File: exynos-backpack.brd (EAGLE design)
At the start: 29 x 52 mm, 17 parts, among them IC1 MIC5335-SPYMT, IC2 TXB0108RGY

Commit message: Route serial section
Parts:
- moved C13 9.41 mm to (18.7, 38.9), turned to 0 degrees
- moved C14 9.03 mm to (21.2, 38.9), turned to 0 degrees
- moved IC1 5.97 mm to (20.0, 36.4), turned to 0 degrees
- moved C12 3.95 mm to (20.0, 34.0), turned to 180 degrees
- moved JP4 3.05 mm to (3.81, 29.0)
- moved JP5 2.13 mm to (25.5, 32.9)
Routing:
- net 1.8V: track 0.00 -> 33.6 mm, vias 0 -> 2
- net ODROID_TXD: track 0.00 -> 26.1 mm
- net ODROID_RXD: track 0.00 -> 20.7 mm
- net V_BATT: track 0.00 -> 6.16 mm
- net 3.3V: track 0.00 -> 5.82 mm
- net IMAGEPROC_RXD: track 0.00 -> 4.09 mm
- net IMAGEPROC_TXD: track 0.00 -> 4.05 mm
- net 3.0V: track 0.00 -> 2.10 mm

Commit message: Delete inner layers
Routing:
- removed copper zone on layer 2, net GND
- removed copper zone on layer 3, net V_BATT

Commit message: Routing complete
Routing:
- net V_BATT: track 6.16 -> 25.2 mm
- added copper zone on layer 1, net 5V
- added copper zone on layer 16, net 5V
- added copper zone on layer 1, net V_BATT
- added copper zone on layer 16, net V_BATT
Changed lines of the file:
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@@
 <setting verticaltext="up"/>
 </settings>
-<grid distance="3" unitdist="mil" unit="mil" style="lines" multiple="1" display="yes" altdistance="1" altunitdist="mil" altunit="mil"/>
+<grid distance="6" unitdist="mil" unit="mil" style="lines" multiple="1" display="yes" altdistance="1" altunitdist="mil" altunit="mil"/>
 <layers>
 <layer number="1" name="Top" color="4" fill="1" visible="yes" active="yes"/>
@@
 <layer number="49" name="Reference" color="7" fill="1" visible="no" active="yes"/>
 <layer number="50" name="dxf" color="7" fill="1" visible="no" active="yes"/>
-<layer number="51" name="tDocu" color="6" fill="1" visible="yes" active="yes"/>
-<layer number="52" name="bDocu" color="7" fill="1" visible="yes" active="yes"/>
+<layer number="51" name="tDocu" color="6" fill="1" visible="no" active="yes"/>
+<layer number="52" name="bDocu" color="7" fill="1" visible="no" active="yes"/>
 <layer number="53" name="tGND_GNDA" color="7" fill="9" visible="no" active="no"/>
 <layer number="54" name="bGND_GNDA" color="1" fill="9" visible="no" active="no"/>
@@
 <contactref element="C15" pad="2"/>
 <contactref element="C16" pad="2"/>
-<polygon width="0.1524" layer="1">
+<polygon width="0.1524" layer="1" rank="6">
 <vertex x="0" y="52"/>
 <vertex x="30.524" y="52"/>
@@
 <vertex x="0" y="9"/>
 </polygon>
-<polygon width="0.1524" layer="16">
+<polygon width="0.1524" layer="16" rank="6">
 <vertex x="0" y="52"/>
-<vertex x="35.096" y="52"/>
-<vertex x="35.096" y="22"/>
+<vertex x="32.048" y="52"/>
+<vertex x="32.048" y="22"/>
 <vertex x="25" y="22"/>
 <vertex x="25" y="0"/>
@@
 <contactref element="JP5" pad="4"/>
 <via x="7.4676" y="49.2252" extent="1-16" drill="0.6" shape="square"/>
+<polygon width="0.1524" layer="1" thermals="no" rank="2">
+<vertex x="0" y="31.5468"/>
+<vertex x="24.9936" y="31.5468"/>
+<vertex x="24.9936" y="5.4864"/>
+<vertex x="15.0876" y="5.4864"/>
+<vertex x="15.0876" y="8.9916"/>
+<vertex x="0" y="8.9916"/>
+</polygon>
+<polygon width="0.1524" layer="16" thermals="no" rank="2">
+<vertex x="0" y="31.5468"/>
+<vertex x="24.9936" y="31.5468"/>
+<vertex x="24.9936" y="5.4864"/>
+<vertex x="15.0876" y="5.4864"/>
+<vertex x="15.0876" y="8.9916"/>
+<vertex x="0" y="8.9916"/>
+</polygon>
 </signal>
 <signal name="1.8V">
@@
 <wire x1="20.4644" y1="34.8662" x2="20.3454" y2="34.7472" width="0.254" layer="1"/>
 <wire x1="20.3454" y1="34.7472" x2="19.4644" y2="34.7472" width="0.254" layer="1"/>
-<wire x1="22.0218" y1="17.2847" x2="19.4818" y2="33.9852" width="0" layer="19" extent="1-1"/>
-<wire x1="22.174" y1="14.1732" x2="22.0218" y2="17.2847" width="0" layer="19" extent="16-16"/>
+<wire x1="19.4818" y1="33.9852" x2="19.4818" y2="29.3878" width="0.508" layer="1"/>
+<wire x1="19.4818" y1="29.3878" x2="17.9832" y2="27.8892" width="0.508" layer="1"/>
+<wire x1="17.9832" y1="27.8892" x2="17.9832" y2="21.3233" width="0.508" layer="1"/>
+<wire x1="17.9832" y1="21.3233" x2="22.0218" y2="17.2847" width="0.508" layer="1"/>
+<polygon width="0.1524" layer="16" thermals="no">
+<vertex x="20.1168" y="6.858"/>
+<vertex x="20.7264" y="6.2484"/>
+<vertex x="24.9936" y="6.2484"/>
+<vertex x="24.9936" y="18.5928"/>
+<vertex x="21.336" y="18.5928"/>
+<vertex x="20.7264" y="17.9832"/>
+<vertex x="20.7264" y="12.3444"/>
+<vertex x="23.4696" y="12.3444"/>
+<vertex x="23.4696" y="9.4488"/>
+<vertex x="21.0312" y="9.4488"/>
+<vertex x="20.1168" y="8.5344"/>
+</polygon>
+<polygon width="0.1524" layer="1" thermals="no">
+<vertex x="20.1168" y="6.858"/>
+<vertex x="20.7264" y="6.2484"/>
+<vertex x="24.9936" y="6.2484"/>
+<vertex x="24.9936" y="18.5928"/>
+<vertex x="21.336" y="18.5928"/>
+<vertex x="20.7264" y="17.9832"/>
+<vertex x="20.7264" y="12.3444"/>
+<vertex x="23.4696" y="12.3444"/>
+<vertex x="23.4696" y="9.4488"/>
+<vertex x="21.0312" y="9.4488"/>
+<vertex x="20.1168" y="8.5344"/>
+</polygon>
 </signal>
 <signal name="3.3V">
@@
 <contactref element="PS1" pad="4"/>
 <contactref element="JP4" pad="2"/>
-<wire x1="5.5628" y1="11.1252" x2="6.96" y2="30.206" width="0" layer="19" extent="16-16"/>
-<wire x1="2.9718" y1="10.9347" x2="5.5628" y2="11.1252" width="0" layer="19" extent="16-16"/>
+<polygon width="0.1524" layer="1" thermals="no">
+<vertex x="7.7724" y="28.956"/>
+<vertex x="5.7912" y="28.956"/>
+<vertex x="4.4196" y="27.5844"/>
+<vertex x="4.4196" y="8.9916"/>
+<vertex x="0" y="8.9916"/>
+<vertex x="0" y="31.5468"/>
+<vertex x="7.7724" y="31.5468"/>
+<vertex x="8.382" y="30.9372"/>
+<vertex x="8.382" y="29.5656"/>
+</polygon>
+<polygon width="0.1524" layer="16" thermals="no">
+<vertex x="6.858" y="12.192"/>
+<vertex x="6.2484" y="12.8016"/>
+<vertex x="1.8288" y="12.8016"/>
+<vertex x="1.2192" y="12.192"/>
+<vertex x="1.2192" y="8.9916"/>
+<vertex x="6.858" y="8.9916"/>
+</polygon>
+<polygon width="0.1524" layer="16" thermals="no">
+<vertex x="7.7724" y="28.956"/>
+<vertex x="5.7912" y="28.956"/>
+<vertex x="4.4196" y="27.5844"/>
+<vertex x="4.4196" y="8.9916"/>
+<vertex x="0" y="8.9916"/>
+<vertex x="0" y="31.5468"/>
+<vertex x="7.7724" y="31.5468"/>
+<vertex x="8.382" y="30.9372"/>
+<vertex x="8.382" y="29.5656"/>
+</polygon>
 </signal>
 <signal name="ODROID_TXD">

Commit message: Arrange silkscreen
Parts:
- removed C14: 1uF, biomimetic:0402-CAP
- JP1: value ODROID -> ODROID UART; device biomimetic:1X04_MOLEX_5267 -> biomimetic:1X04_MOLEX_5267_NOSILK
- JP3: value JST-RCY-MALE-NOSILK -> BATTERY
- JP4: value JST-RCY-FEMALE-NOSILK -> ODROID 5V
- JP5: value ODROID CONSOLE -> CONSOLE
- moved U$12 66.9 mm to (7.47, 45.9)
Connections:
- removed net 3.0V: C14.1, IC1.5
- net GND: now also IC1.3; no longer C14.2
- net V_BATT: no longer IC1.3
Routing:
- net 3.0V: track 2.10 -> 0.00 mm
- net V_BATT: track 25.2 -> 24.5 mm
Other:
- board text added: "Biomimetic Millisystems Laboratory"
- board text added: "Design by: Ryan Julian"
- board text added: "Exynos Backpack v1.0 Rev. A 2013.02.27"
- board text removed: "2013.02.16"
- board text removed: "Biomimetic"
- board text removed: "Exynos Backpack 1.0 Rev. A"
- board text removed: "Laboratory"
- board text removed: "Millisystems"
- board text removed: "Ryan Julian"

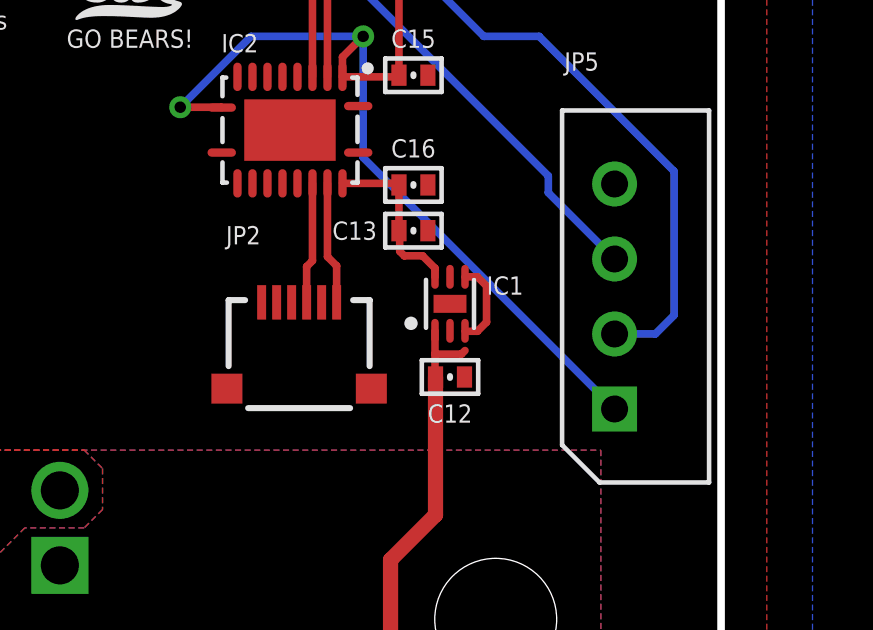
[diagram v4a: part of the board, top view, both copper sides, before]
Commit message: Disable 3.0v supply
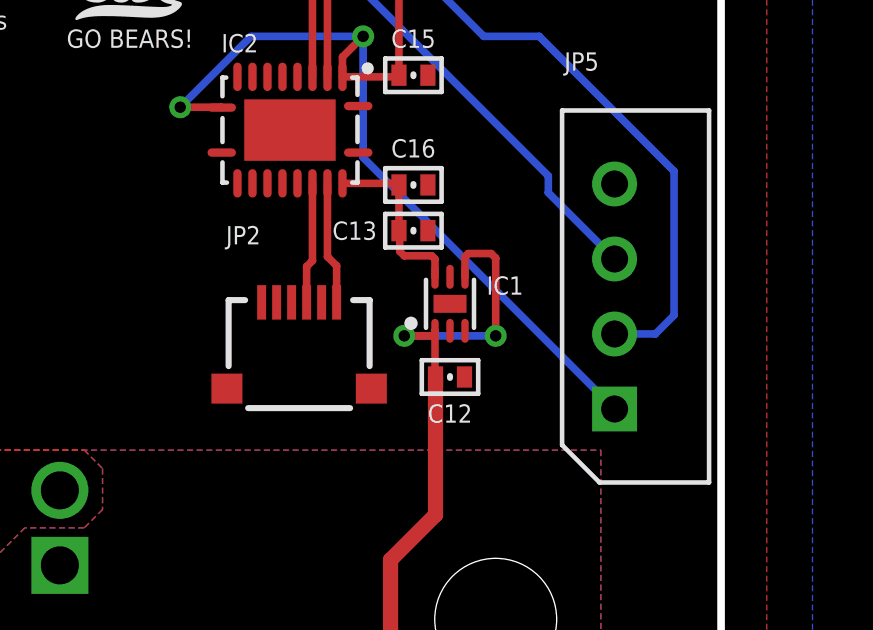
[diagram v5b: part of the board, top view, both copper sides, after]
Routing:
- net V_BATT: track 24.5 -> 29.2 mm, vias 0 -> 2
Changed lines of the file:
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@@
 <grid distance="6" unitdist="mil" unit="mil" style="lines" multiple="1" display="yes" altdistance="1" altunitdist="mil" altunit="mil"/>
 <layers>
-<layer number="1" name="Top" color="4" fill="1" visible="no" active="yes"/>
+<layer number="1" name="Top" color="4" fill="1" visible="yes" active="yes"/>
 <layer number="2" name="Route2" color="1" fill="3" visible="no" active="yes"/>
 <layer number="3" name="Route3" color="4" fill="3" visible="no" active="yes"/>
@@
 <layer number="14" name="Route14" color="1" fill="6" visible="no" active="no"/>
 <layer number="15" name="Route15" color="4" fill="6" visible="no" active="no"/>
-<layer number="16" name="Bottom" color="1" fill="1" visible="no" active="yes"/>
+<layer number="16" name="Bottom" color="1" fill="1" visible="yes" active="yes"/>
 <layer number="17" name="Pads" color="2" fill="1" visible="no" active="yes"/>
-<layer number="18" name="Vias" color="2" fill="1" visible="no" active="yes"/>
-<layer number="19" name="Unrouted" color="6" fill="1" visible="no" active="yes"/>
+<layer number="18" name="Vias" color="2" fill="1" visible="yes" active="yes"/>
+<layer number="19" name="Unrouted" color="6" fill="1" visible="yes" active="yes"/>
 <layer number="20" name="Dimension" color="15" fill="1" visible="yes" active="yes"/>
 <layer number="21" name="tPlace" color="16" fill="1" visible="no" active="yes"/>
@@
 <layer number="27" name="tValues" color="7" fill="1" visible="no" active="yes"/>
 <layer number="28" name="bValues" color="7" fill="1" visible="yes" active="yes"/>
-<layer number="29" name="tStop" color="7" fill="3" visible="no" active="yes"/>
+<layer number="29" name="tStop" color="7" fill="3" visible="yes" active="yes"/>
 <layer number="30" name="bStop" color="7" fill="6" visible="yes" active="yes"/>
 <layer number="31" name="tCream" color="7" fill="4" visible="no" active="yes"/>
@@
 </polygon>
 <contactref element="IC1" pad="3"/>
-<wire x1="19.9644" y1="35.5236" x2="20.4644" y2="35.5236" width="0" layer="19" extent="1-1"/>
 </signal>
 <signal name="1.8V">
@@
 <contactref element="PS1" pad="2"/>
 <contactref element="JP3" pad="2"/>
-<wire x1="19.4644" y1="35.5236" x2="19.4644" y2="34.7472" width="0.254" layer="1"/>
-<wire x1="19.4644" y1="34.7472" x2="19.4644" y2="34.0026" width="0.254" layer="1"/>
+<wire x1="19.4644" y1="35.5236" x2="19.4644" y2="34.0026" width="0.254" layer="1"/>
 <wire x1="19.4644" y1="34.0026" x2="19.4818" y2="33.9852" width="0.254" layer="1"/>
-<wire x1="20.4644" y1="37.3236" x2="20.8788" y2="37.3236" width="0.254" layer="1"/>
-<wire x1="20.8788" y1="37.3236" x2="21.1836" y2="37.0188" width="0.254" layer="1"/>
-<wire x1="21.1836" y1="37.0188" x2="21.1836" y2="35.814" width="0.254" layer="1"/>
-<wire x1="21.1836" y1="35.814" x2="20.8788" y2="35.5092" width="0.254" layer="1"/>
-<wire x1="20.8788" y1="35.5092" x2="20.4644" y2="35.5092" width="0.254" layer="1"/>
-<wire x1="20.4644" y1="34.8662" x2="20.3454" y2="34.7472" width="0.254" layer="1"/>
-<wire x1="20.3454" y1="34.7472" x2="19.4644" y2="34.7472" width="0.254" layer="1"/>
 <wire x1="19.4818" y1="33.9852" x2="19.4818" y2="29.3878" width="0.508" layer="1"/>
 <wire x1="19.4818" y1="29.3878" x2="17.9832" y2="27.8892" width="0.508" layer="1"/>
@@
 <vertex x="20.1168" y="8.5344"/>
 </polygon>
-<wire x1="20.4644" y1="34.8662" x2="20.4644" y2="35.5092" width="0" layer="19" extent="1-1"/>
+<via x="21.4884" y="35.3568" extent="1-16" drill="0.381"/>
+<wire x1="20.4644" y1="37.3236" x2="20.4644" y2="37.9904" width="0.254" layer="1"/>
+<wire x1="20.4644" y1="37.9904" x2="20.574" y2="38.1" width="0.254" layer="1"/>
+<wire x1="20.574" y1="38.1" x2="21.336" y2="38.1" width="0.254" layer="1"/>
+<wire x1="21.336" y1="38.1" x2="21.4884" y2="37.9476" width="0.254" layer="1"/>
+<wire x1="21.4884" y1="37.9476" x2="21.4884" y2="35.3568" width="0.254" layer="1"/>
+<via x="18.4404" y="35.3568" extent="1-16" drill="0.381"/>
+<wire x1="21.4884" y1="35.3568" x2="18.4404" y2="35.3568" width="0.254" layer="16"/>
+<wire x1="19.4644" y1="35.5236" x2="19.4644" y2="35.3568" width="0.254" layer="1"/>
+<wire x1="19.4644" y1="35.3568" x2="18.4404" y2="35.3568" width="0.254" layer="1"/>
 </signal>
 <signal name="3.3V">
@@
 <wire x1="18.2088" y1="40.4398" x2="16.3804" y2="40.4398" width="0.254" layer="1"/>
 <wire x1="18.2626" y1="40.386" x2="18.2626" y2="38.862" width="0.254" layer="1"/>
-<wire x1="19.4644" y1="37.3236" x2="19.4644" y2="37.6094" width="0.254" layer="1"/>
-<wire x1="19.4644" y1="37.6094" x2="19.05" y2="38.0238" width="0.254" layer="1"/>
-<wire x1="19.05" y1="38.0238" x2="18.4404" y2="38.0238" width="0.254" layer="1"/>
+<wire x1="19.4644" y1="37.3236" x2="19.4644" y2="37.9142" width="0.254" layer="1"/>
+<wire x1="19.4644" y1="37.9142" x2="19.3548" y2="38.0238" width="0.254" layer="1"/>
+<wire x1="19.3548" y1="38.0238" x2="18.4404" y2="38.0238" width="0.254" layer="1"/>
 <wire x1="18.4404" y1="38.0238" x2="18.288" y2="38.1762" width="0.254" layer="1"/>
 <wire x1="18.288" y1="38.1762" x2="18.288" y2="38.8366" width="0.254" layer="1"/>

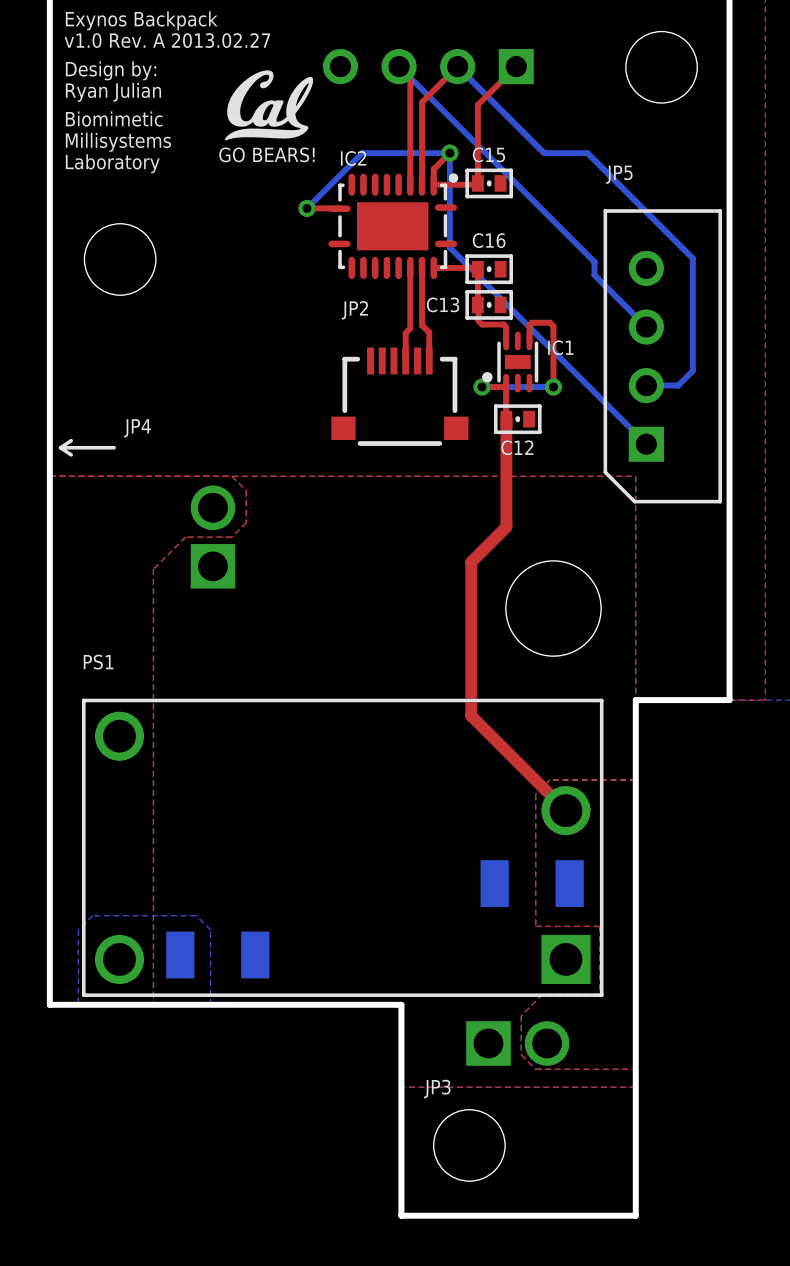
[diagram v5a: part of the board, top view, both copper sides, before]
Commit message: Renumber components for silk
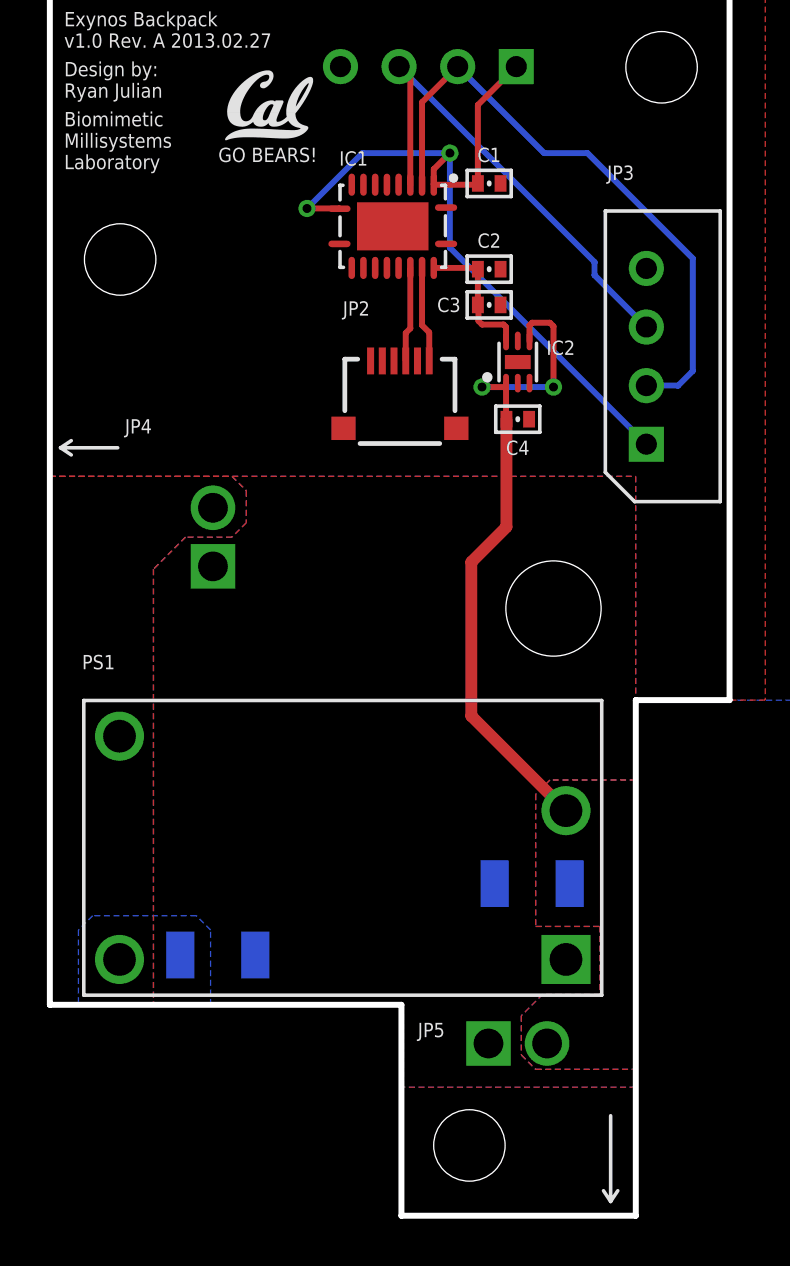
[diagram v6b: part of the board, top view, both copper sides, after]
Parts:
- IC1: value MIC5335-SPYMT -> TXB0108RGY; device biomimetic:MLF-6 -> biomimetic:R-PVQFN-N20
- IC2: value TXB0108RGY -> MIC5335-SPYMT; device biomimetic:R-PVQFN-N20 -> biomimetic:MLF-6
- JP3: value BATTERY -> CONSOLE; device biomimetic:JST-RCY-MALE_NOSILK -> biomimetic:1X04_MOLEX_5267
- JP5: value CONSOLE -> BATTERY; device biomimetic:1X04_MOLEX_5267 -> biomimetic:JST-RCY-MALE_NOSILK
- moved JP3 33.4 mm to (25.5, 32.9), turned to 90 degrees
- moved JP5 33.4 mm to (20.0, 0.00), turned to 180 degrees
- moved IC1 7.87 mm to (14.6, 42.2), turned to 180 degrees
- moved IC2 7.87 mm to (20.0, 36.4), turned to 0 degrees
- renumbered C10 to C101, C11 to C100, C12 to C4, C13 to C3, C15 to C1, C16 to C2, U$12 to $$U$1
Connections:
- net 1.8V: now also IC1.10, IC1.2, JP3.1; no longer IC2.10, IC2.2, JP5.1
- net 3.3V: now also IC1.19, IC2.6; no longer IC1.6, IC2.19
- net GND: now also IC1.1, IC1.11, IC1.12, IC1.13, IC1.14, IC1.15, IC1.16, IC1.20, IC1.5, IC1.6, IC1.7, IC1.8, IC1.9, IC2.2, IC2.3, JP3.4, JP5.1; no longer IC1.2, IC1.3, IC2.1, IC2.11, IC2.12, IC2.13, IC2.14, IC2.15, IC2.16, IC2.20, IC2.5, IC2.6, IC2.7, IC2.8, IC2.9, JP3.1, JP5.4
- net IMAGEPROC_RXD: now also IC1.18; no longer IC2.18
- net IMAGEPROC_TXD: now also IC1.17; no longer IC2.17
- net ODROID_RXD: now also IC1.4, JP3.3; no longer IC2.4, JP5.3
- net ODROID_TXD: now also IC1.3, JP3.2; no longer IC2.3, JP5.2
- net V_BATT: now also IC2.1, IC2.4, JP5.2; no longer IC1.1, IC1.4, JP3.2
